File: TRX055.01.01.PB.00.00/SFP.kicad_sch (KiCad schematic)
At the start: 1 part, among them J5 SFP

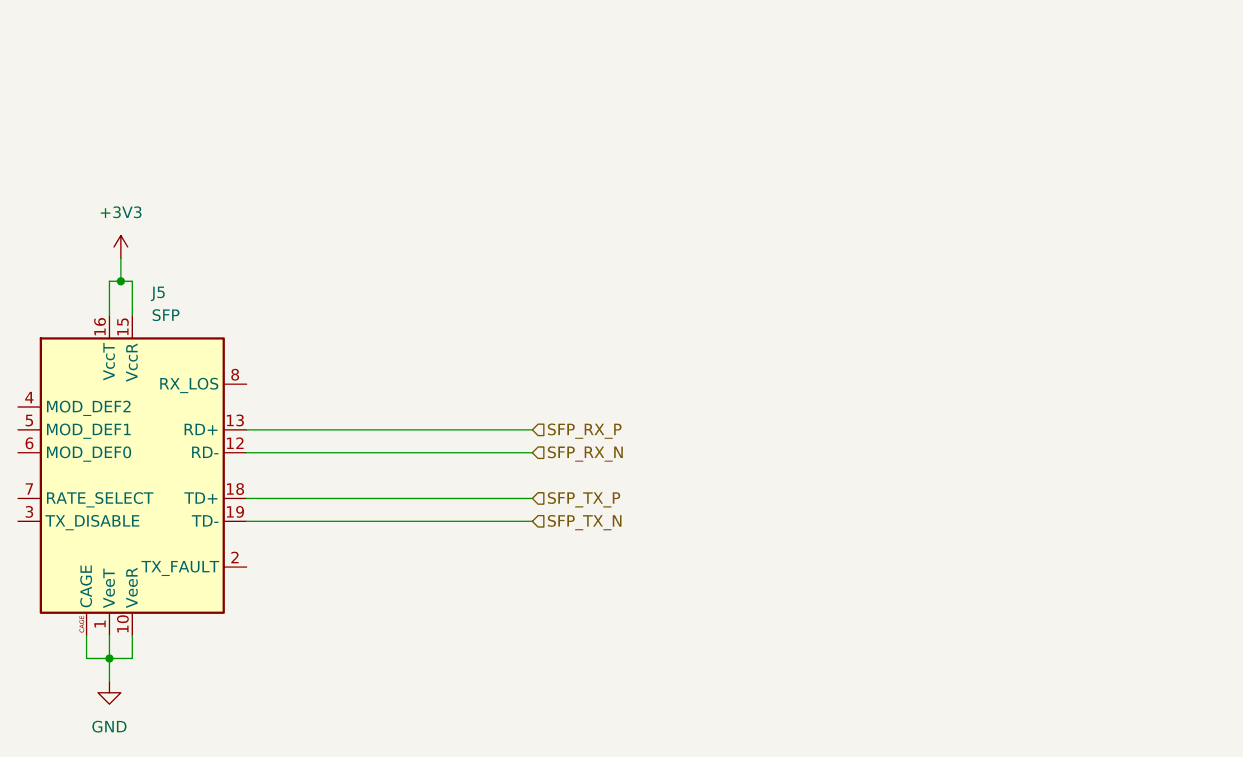
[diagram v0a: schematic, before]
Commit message: + add clocks + add PSU
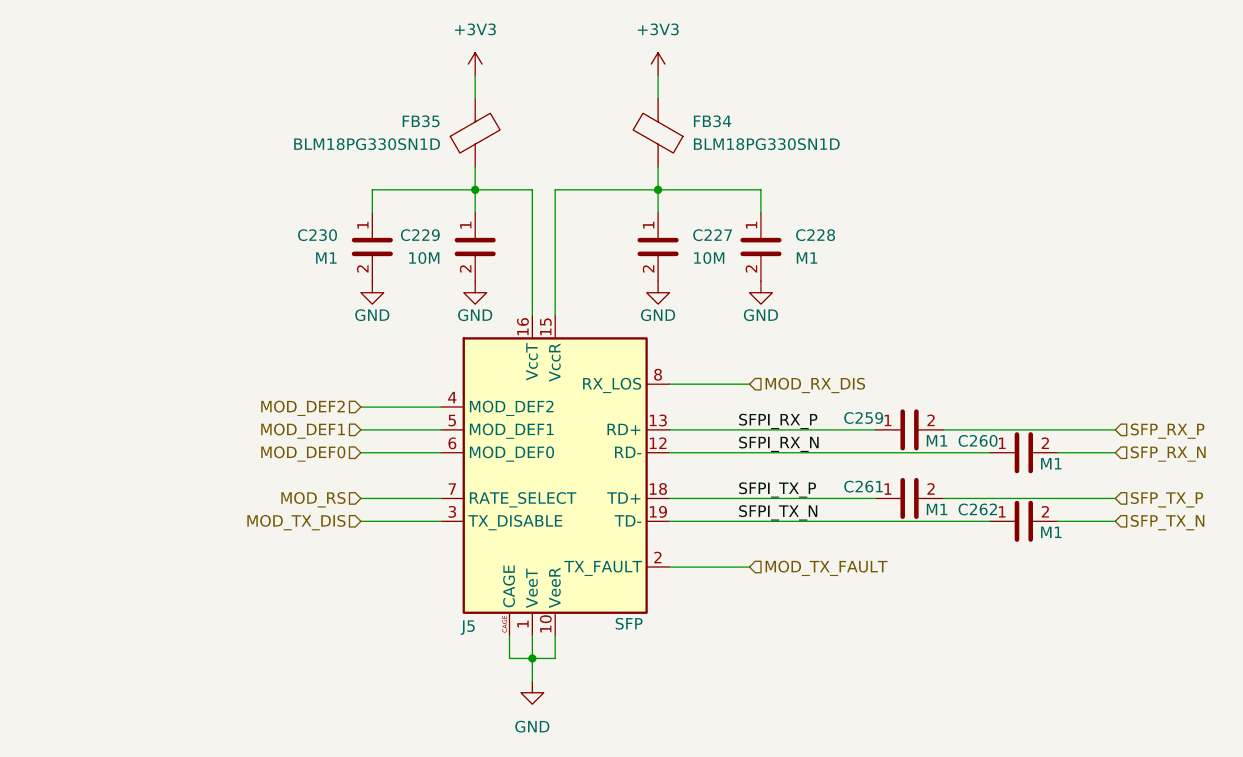
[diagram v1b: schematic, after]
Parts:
- added C227, C229: 10M, Capacitor_SMD:C_0603_1608Metric, symbol PPA-Pasive:Cap
- added C228, C230, C259, C260, C261, C262: M1, Capacitor_SMD:C_0201_0603Metric, symbol PPA-Pasive:Cap
- added FB34, FB35: BLM18PG330SN1D, Inductor_SMD:L_0603_1608Metric, symbol Device:FerriteBead
- J5: JLCPCB Part # (none) -> C42418480
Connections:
- net +3V3: now also FB34.2, FB35.2; no longer J5.15 (VccR), J5.16 (VccT)
- net GND: now also C227.2, C228.2, C229.2, C230.2
- net SFP_RX_N: now also C260.2; no longer J5.12 (RD-)
- net SFP_RX_P: now also C259.2; no longer J5.13 (RD+)
- net SFP_TX_N: now also C262.2; no longer J5.19 (TD-)
- net SFP_TX_P: now also C261.2; no longer J5.18 (TD+)
- net MOD_TX_FAULT: now reaches J5.2 (TX_FAULT)
- net MOD_TX_DIS: now reaches J5.3 (TX_DISABLE)
- net MOD_DEF2: now reaches J5.4 (MOD_DEF2)
- net MOD_DEF1: now reaches J5.5 (MOD_DEF1)
- net MOD_DEF0: now reaches J5.6 (MOD_DEF0)
- net MOD_RS: now reaches J5.7 (RATE_SELECT)
- net MOD_RX_DIS: now reaches J5.8 (RX_LOS)
- new net: C229.1, C230.1, FB35.1, J5.16 (VccT)
- new net: C227.1, C228.1, FB34.1, J5.15 (VccR)
- new net SFPI_RX_N: C260.1, J5.12 (RD-)
- new net SFPI_RX_P: C259.1, J5.13 (RD+)
- new net SFPI_TX_N: C262.1, J5.19 (TD-)
- new net SFPI_TX_P: C261.1, J5.18 (TD+)
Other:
- moved on the sheet: J5

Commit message: V0.1 - production, added brig-up comments
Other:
- company: (none) -> Tronex s.r.o. / Tronex Group USA LLC
- title: (none) -> TRNX SDR Carrier board
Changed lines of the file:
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@@
 	(generator_version "9.0")
 	(paper "A4")
+	(title_block
+		(title "TRNX SDR Carrier board")
+		(date "2025-11-18")
+		(rev "0.1")
+		(company "Tronex s.r.o. / Tronex Group USA LLC")
+	)
 	(junction
 		(at 157.48 66.04)
